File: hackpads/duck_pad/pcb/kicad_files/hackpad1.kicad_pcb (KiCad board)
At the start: 2 copper layers, 97.6 x 97.6 mm, 40 parts, among them U2 MCU_Seeed_XIAO_RP2040

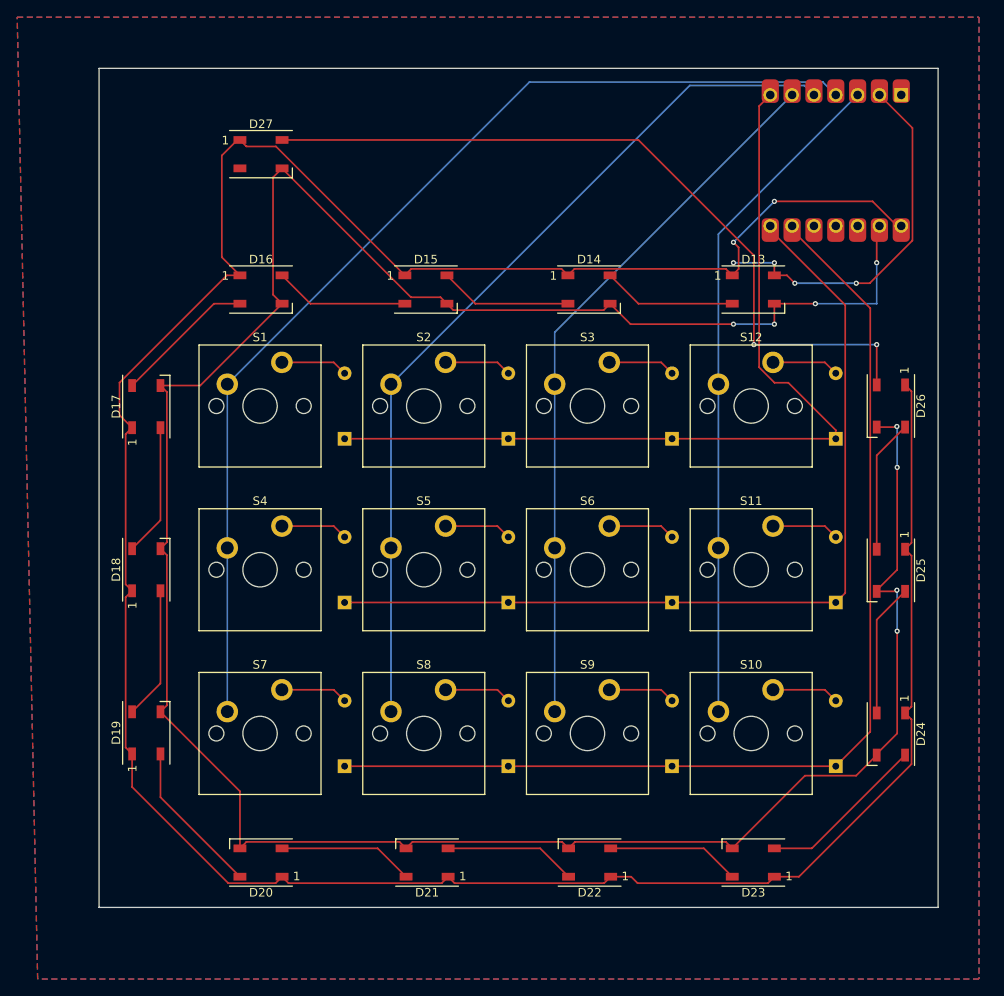
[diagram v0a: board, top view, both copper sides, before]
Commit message: SMDs removed
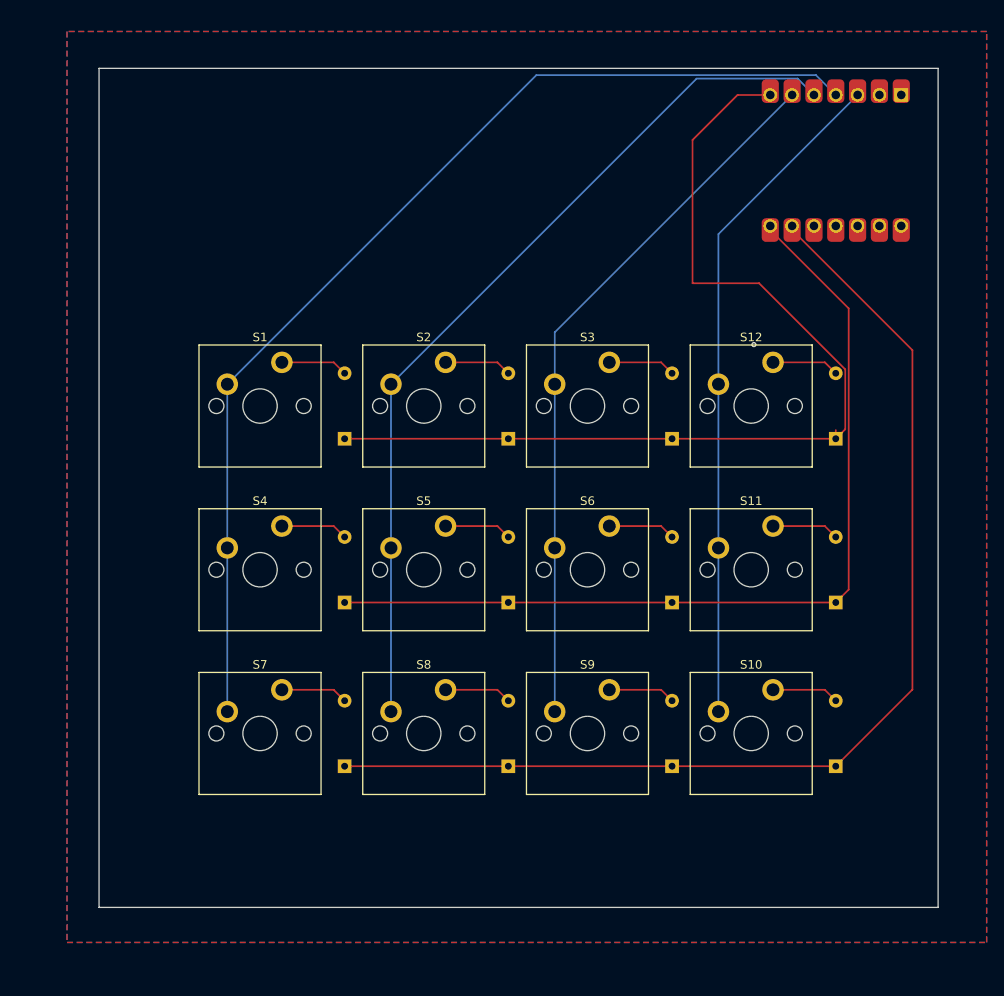
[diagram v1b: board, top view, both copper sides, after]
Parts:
- removed D13, D14, D15, D16, D17, D18, D19, D20, D21, D22, D23, D24, D25, D26, D27: LED_WS2812B, ScottoKeebs_Components:LED_WS2812B
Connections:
- U2 pad 14: Net-(D13-VDD) -> unconnected-(U2-5V-Pad14)
- U2 pad 2: Net-(D13-DIN) -> unconnected-(U2-PA4_A1_D1-Pad2)
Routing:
- net Net-(D13-VDD): track 326.7 -> 0.00 mm, vias 2 -> 0
- net GND: track 308.2 -> 0.00 mm, vias 8 -> 0
- net Net-(D26-DOUT): track 89.8 -> 0.00 mm, vias 2 -> 0
- net Net-(D13-DIN): track 43.3 -> 0.00 mm, vias 4 -> 0
- net Net-(D23-DOUT): track 19.7 -> 0.00 mm
- net Net-(D19-DOUT): track 18.1 -> 0.00 mm
- net Net-(D16-DOUT): track 16.5 -> 0.00 mm
- net Net-(D20-DOUT): track 15.8 -> 0.00 mm
- net Net-(D15-DOUT): track 15.7 -> 0.00 mm
- net Net-(D13-DOUT): track 15.6 -> 0.00 mm
- net Net-(D25-DOUT): track 15.6 -> 0.00 mm
- net Net-(D22-DOUT): track 15.5 -> 0.00 mm
- net Net-(D24-DOUT): track 15.5 -> 0.00 mm
- net Net-(D17-DOUT): track 15.4 -> 0.00 mm
- net Net-(D18-DOUT): track 15.4 -> 0.00 mm
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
